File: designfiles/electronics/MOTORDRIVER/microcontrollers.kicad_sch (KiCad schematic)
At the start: 29 parts, among them IC8 ATSAME53J18A-MF, U5 ATSAMD11D14A-M

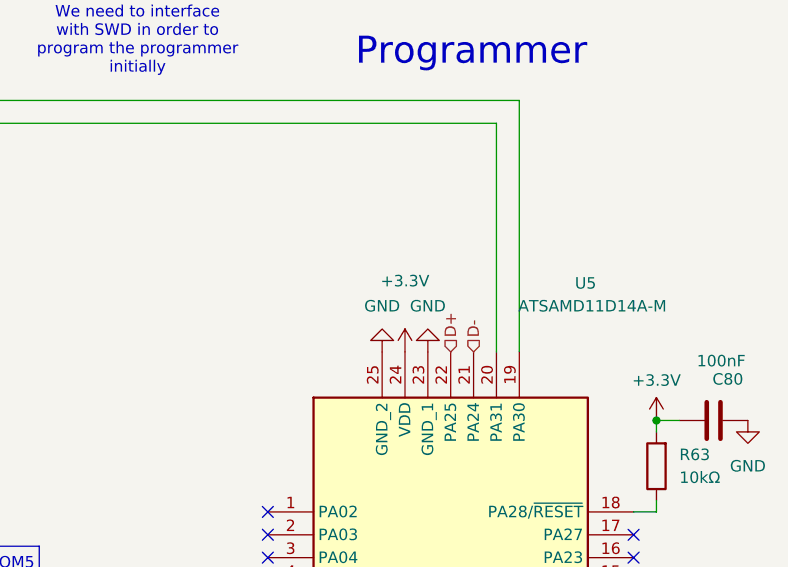
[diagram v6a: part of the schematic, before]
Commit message: added design rules from pcbway, we need to redo some work to fit the design rules
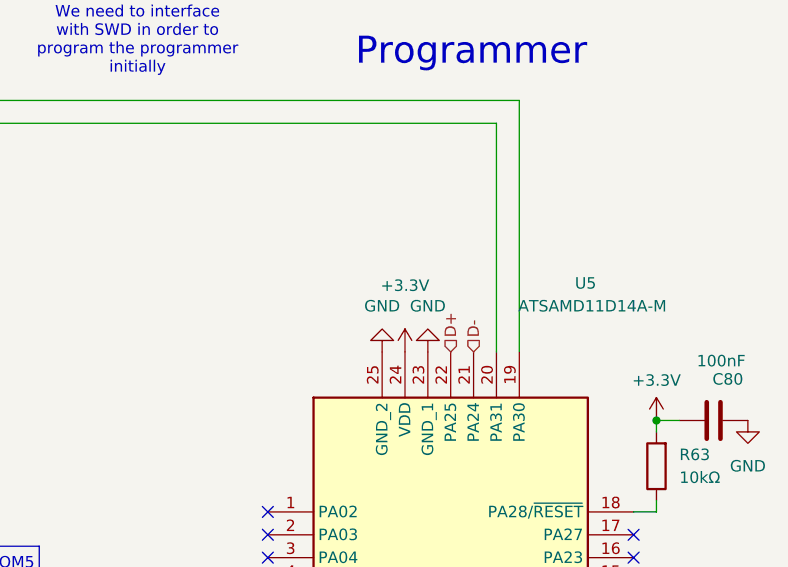
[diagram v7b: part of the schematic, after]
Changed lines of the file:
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@@
 		(dnp no)
 		(fields_autoplaced yes)
-		(property "Reference" "#PWR0148"
+		(property "Reference" "#PWR0152"
 			(at 148.59 73.66 0)
 			(effects
@@
 			(project "motordriver"
 				(path "/c7634e88-16d1-45ec-9aac-9c841e03cf6d/9ebbb593-eaf1-4a56-ba2a-164e20b1d55e"
-					(reference "#PWR0148")
+					(reference "#PWR0152")
 					(unit 1)
 				)
@@
 		(dnp no)
 		(fields_autoplaced yes)
-		(property "Reference" "#PWR0152"
+		(property "Reference" "#PWR0156"
 			(at 180.34 92.71 0)
 			(effects
@@
 			(project "motordriver"
 				(path "/c7634e88-16d1-45ec-9aac-9c841e03cf6d/9ebbb593-eaf1-4a56-ba2a-164e20b1d55e"
-					(reference "#PWR0152")
+					(reference "#PWR0156")
 					(unit 1)
 				)
@@
 		(dnp no)
 		(fields_autoplaced yes)
-		(property "Reference" "#PWR0141"
+		(property "Reference" "#PWR0145"
 			(at 85.09 48.26 0)
 			(effects
@@
 			(project "motordriver"
 				(path "/c7634e88-16d1-45ec-9aac-9c841e03cf6d/9ebbb593-eaf1-4a56-ba2a-164e20b1d55e"
-					(reference "#PWR0141")
+					(reference "#PWR0145")
 					(unit 1)
 				)
@@
 		(dnp no)
 		(fields_autoplaced yes)
-		(property "Reference" "#PWR0151"
+		(property "Reference" "#PWR0155"
 			(at 170.18 90.17 0)
 			(effects
@@
 			(project "motordriver"
 				(path "/c7634e88-16d1-45ec-9aac-9c841e03cf6d/9ebbb593-eaf1-4a56-ba2a-164e20b1d55e"
-					(reference "#PWR0151")
+					(reference "#PWR0155")
 					(unit 1)
 				)
@@
 		(dnp no)
 		(fields_autoplaced yes)
-		(property "Reference" "#PWR0160"
+		(property "Reference" "#PWR0164"
 			(at 278.13 86.36 0)
 			(effects
@@
 			(project "motordriver"
 				(path "/c7634e88-16d1-45ec-9aac-9c841e03cf6d/9ebbb593-eaf1-4a56-ba2a-164e20b1d55e"
-					(reference "#PWR0160")
+					(reference "#PWR0164")
 					(unit 1)
 				)
@@
 		(dnp no)
 		(fields_autoplaced yes)
-		(property "Reference" "#PWR0143"
+		(property "Reference" "#PWR0147"
 			(at 85.09 73.66 0)
 			(effects
@@
 			(project "motordriver"
 				(path "/c7634e88-16d1-45ec-9aac-9c841e03cf6d/9ebbb593-eaf1-4a56-ba2a-164e20b1d55e"
-					(reference "#PWR0143")
+					(reference "#PWR0147")
 					(unit 1)
 				)
@@
 		(dnp no)
 		(fields_autoplaced yes)
-		(property "Reference" "#PWR0135"
+		(property "Reference" "#PWR0139"
 			(at 26.67 144.78 0)
 			(effects
@@
 			(project "motordriver"
 				(path "/c7634e88-16d1-45ec-9aac-9c841e03cf6d/9ebbb593-eaf1-4a56-ba2a-164e20b1d55e"
-					(reference "#PWR0135")
+					(reference "#PWR0139")
 					(unit 1)
 				)
@@
 		(dnp no)
 		(fields_autoplaced yes)
-		(property "Reference" "#PWR0140"
+		(property "Reference" "#PWR0144"
 			(at 85.09 35.56 0)
 			(effects
@@
 			(project "motordriver"
 				(path "/c7634e88-16d1-45ec-9aac-9c841e03cf6d/9ebbb593-eaf1-4a56-ba2a-164e20b1d55e"
-					(reference "#PWR0140")
+					(reference "#PWR0144")
 					(unit 1)
 				)
@@
 		(dnp no)
 		(fields_autoplaced yes)
-		(property "Reference" "#PWR0150"
+		(property "Reference" "#PWR0154"
 			(at 156.21 48.26 0)
 			(effects
@@
 			(project "motordriver"
 				(path "/c7634e88-16d1-45ec-9aac-9c841e03cf6d/9ebbb593-eaf1-4a56-ba2a-164e20b1d55e"
-					(reference "#PWR0150")
+					(reference "#PWR0154")
 					(unit 1)
 				)
@@
 		(dnp no)
 		(fields_autoplaced yes)
-		(property "Reference" "#PWR0138"
+		(property "Reference" "#PWR0142"
 			(at 68.58 144.78 0)
 			(effects
@@
 			(project "motordriver"
 				(path "/c7634e88-16d1-45ec-9aac-9c841e03cf6d/9ebbb593-eaf1-4a56-ba2a-164e20b1d55e"
-					(reference "#PWR0138")
+					(reference "#PWR0142")
 					(unit 1)
 				)
@@
 		(dnp no)
 		(fields_autoplaced yes)
-		(property "Reference" "#PWR0156"
+		(property "Reference" "#PWR0160"
 			(at 237.49 66.04 0)
 			(effects
@@
 			(project "motordriver"
 				(path "/c7634e88-16d1-45ec-9aac-9c841e03cf6d/9ebbb593-eaf1-4a56-ba2a-164e20b1d55e"
-					(reference "#PWR0156")
+					(reference "#PWR0160")
 					(unit 1)
 				)
@@
 		(dnp no)
 		(fields_autoplaced yes)
-		(property "Reference" "#PWR0142"
+		(property "Reference" "#PWR0146"
 			(at 85.09 59.69 0)
 			(effects
@@
 			(project "motordriver"
 				(path "/c7634e88-16d1-45ec-9aac-9c841e03cf6d/9ebbb593-eaf1-4a56-ba2a-164e20b1d55e"
-					(reference "#PWR0142")
+					(reference "#PWR0146")
 					(unit 1)
 				)
@@
 		(dnp no)
 		(fields_autoplaced yes)
-		(property "Reference" "#PWR0139"
+		(property "Reference" "#PWR0143"
 			(at 83.82 144.78 0)
 			(effects
@@
 			(project "motordriver"
 				(path "/c7634e88-16d1-45ec-9aac-9c841e03cf6d/9ebbb593-eaf1-4a56-ba2a-164e20b1d55e"
-					(reference "#PWR0139")
+					(reference "#PWR0143")
 					(unit 1)
 				)
@@
 		(dnp no)
 		(fields_autoplaced yes)
-		(property "Reference" "#PWR0149"
+		(property "Reference" "#PWR0153"
 			(at 153.67 63.5 0)
 			(effects
@@
 			(project "motordriver"
 				(path "/c7634e88-16d1-45ec-9aac-9c841e03cf6d/9ebbb593-eaf1-4a56-ba2a-164e20b1d55e"
-					(reference "#PWR0149")
+					(reference "#PWR0153")
 					(unit 1)
 				)
@@
 		(on_board yes)
 		(dnp no)
-		(property "Reference" "#PWR0147"
+		(property "Reference" "#PWR0151"
 			(at 138.43 152.4 0)
 			(effects
@@
 			(project "motordriver"
 				(path "/c7634e88-16d1-45ec-9aac-9c841e03cf6d/9ebbb593-eaf1-4a56-ba2a-164e20b1d55e"
-					(reference "#PWR0147")
+					(reference "#PWR0151")
 					(unit 1)
 				)
@@
 		(dnp no)
 		(fields_autoplaced yes)
-		(property "Reference" "#PWR0159"
+		(property "Reference" "#PWR0163"
 			(at 267.97 83.82 0)
 			(effects
@@
 			(project "motordriver"
 				(path "/c7634e88-16d1-45ec-9aac-9c841e03cf6d/9ebbb593-eaf1-4a56-ba2a-164e20b1d55e"
-					(reference "#PWR0159")
+					(reference "#PWR0163")
 					(unit 1)
 				)
@@
 		(on_board yes)
 		(dnp no)
-		(property "Reference" "#PWR0157"
+		(property "Reference" "#PWR0161"
 			(at 240.03 76.2 0)
 			(effects
@@
 		)
 		(property "Value" "+3.3V"
-			(at 240.03 64.516 0)
+			(at 240.03 65.024 0)
 			(effects
 				(font
@@
 			(project "motordriver"
 				(path "/c7634e88-16d1-45ec-9aac-9c841e03cf6d/9ebbb593-eaf1-4a56-ba2a-164e20b1d55e"
-					(reference "#PWR0157")
+					(reference "#PWR0161")
 					(unit 1)
 				)
@@
 		(dnp no)
 		(fields_autoplaced yes)
-		(property "Reference" "#PWR0136"
+		(property "Reference" "#PWR0140"
 			(at 40.64 144.78 0)
 			(effects
@@
 			(project "motordriver"
 				(path "/c7634e88-16d1-45ec-9aac-9c841e03cf6d/9ebbb593-eaf1-4a56-ba2a-164e20b1d55e"
-					(reference "#PWR0136")
+					(reference "#PWR0140")
 					(unit 1)
 				)
@@
 		(dnp no)
 		(fields_autoplaced yes)
-		(property "Reference" "#PWR0145"
+		(property "Reference" "#PWR0149"
 			(at 121.92 107.95 0)
 			(effects
@@
 			(project "motordriver"
 				(path "/c7634e88-16d1-45ec-9aac-9c841e03cf6d/9ebbb593-eaf1-4a56-ba2a-164e20b1d55e"
-					(reference "#PWR0145")
+					(reference "#PWR0149")
 					(unit 1)
 				)
@@
 		(dnp no)
 		(fields_autoplaced yes)
-		(property "Reference" "#PWR0155"
+		(property "Reference" "#PWR0159"
 			(at 176.53 67.31 0)
 			(effects
@@
 			(project "motordriver"
 				(path "/c7634e88-16d1-45ec-9aac-9c841e03cf6d/9ebbb593-eaf1-4a56-ba2a-164e20b1d55e"
-					(reference "#PWR0155")
+					(reference "#PWR0159")
 					(unit 1)
 				)
@@
 		(dnp no)
 		(fields_autoplaced yes)
-		(property "Reference" "#PWR0137"
+		(property "Reference" "#PWR0141"
 			(at 54.61 144.78 0)
 			(effects
@@
 			(project "motordriver"
 				(path "/c7634e88-16d1-45ec-9aac-9c841e03cf6d/9ebbb593-eaf1-4a56-ba2a-164e20b1d55e"
-					(reference "#PWR0137")
+					(reference "#PWR0141")
 					(unit 1)
 				)
@@
 		(on_board yes)
 		(dnp no)
-		(property "Reference" "#PWR0146"
+		(property "Reference" "#PWR0150"
 			(at 135.89 142.24 0)
 			(effects
@@
 			(project "motordriver"
 				(path "/c7634e88-16d1-45ec-9aac-9c841e03cf6d/9ebbb593-eaf1-4a56-ba2a-164e20b1d55e"
-					(reference "#PWR0146")
+					(reference "#PWR0150")
 					(unit 1)
 				)
@@
 		(dnp no)
 		(fields_autoplaced yes)
-		(property "Reference" "#PWR0144"
+		(property "Reference" "#PWR0148"
 			(at 111.76 105.41 0)
 			(effects
@@
 			(project "motordriver"
 				(path "/c7634e88-16d1-45ec-9aac-9c841e03cf6d/9ebbb593-eaf1-4a56-ba2a-164e20b1d55e"
-					(reference "#PWR0144")
+					(reference "#PWR0148")
 					(unit 1)
 				)
@@
 		(dnp no)
 		(fields_autoplaced yes)
-		(property "Reference" "#PWR0158"
+		(property "Reference" "#PWR0162"
 			(at 242.57 66.04 0)
 			(effects
@@
 			(project "motordriver"
 				(path "/c7634e88-16d1-45ec-9aac-9c841e03cf6d/9ebbb593-eaf1-4a56-ba2a-164e20b1d55e"
-					(reference "#PWR0158")
+					(reference "#PWR0162")
 					(unit 1)
 				)
@@
 		(dnp no)
 		(fields_autoplaced yes)
-		(property "Reference" "#PWR0154"
+		(property "Reference" "#PWR0158"
 			(at 180.34 128.27 0)
 			(effects
@@
 			(project "motordriver"
 				(path "/c7634e88-16d1-45ec-9aac-9c841e03cf6d/9ebbb593-eaf1-4a56-ba2a-164e20b1d55e"
-					(reference "#PWR0154")
+					(reference "#PWR0158")
 					(unit 1)
 				)
@@
 		(dnp no)
 		(fields_autoplaced yes)
-		(property "Reference" "#PWR0153"
+		(property "Reference" "#PWR0157"
 			(at 170.18 125.73 0)
 			(effects
@@
 			(project "motordriver"
 				(path "/c7634e88-16d1-45ec-9aac-9c841e03cf6d/9ebbb593-eaf1-4a56-ba2a-164e20b1d55e"
-					(reference "#PWR0153")
+					(reference "#PWR0157")
 					(unit 1)
 				)

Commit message: worked on pcb
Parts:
- renumbered C65 to C67, C66 to C68, C67 to C69, C68 to C70, C69 to C71, C70 to C72, C71 to C73, C72 to C74, C73 to C75, C74 to C76, C75 to C77, C76 to C78, C77 to C79, C78 to C80, C79 to C81, C80 to C82, U5 to U6
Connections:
- net GND: now also IC8.65 (EP)
- no-connect marks 30 -> 29
